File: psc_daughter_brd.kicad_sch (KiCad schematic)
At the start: 5 parts, among them J1 61082-061400LF

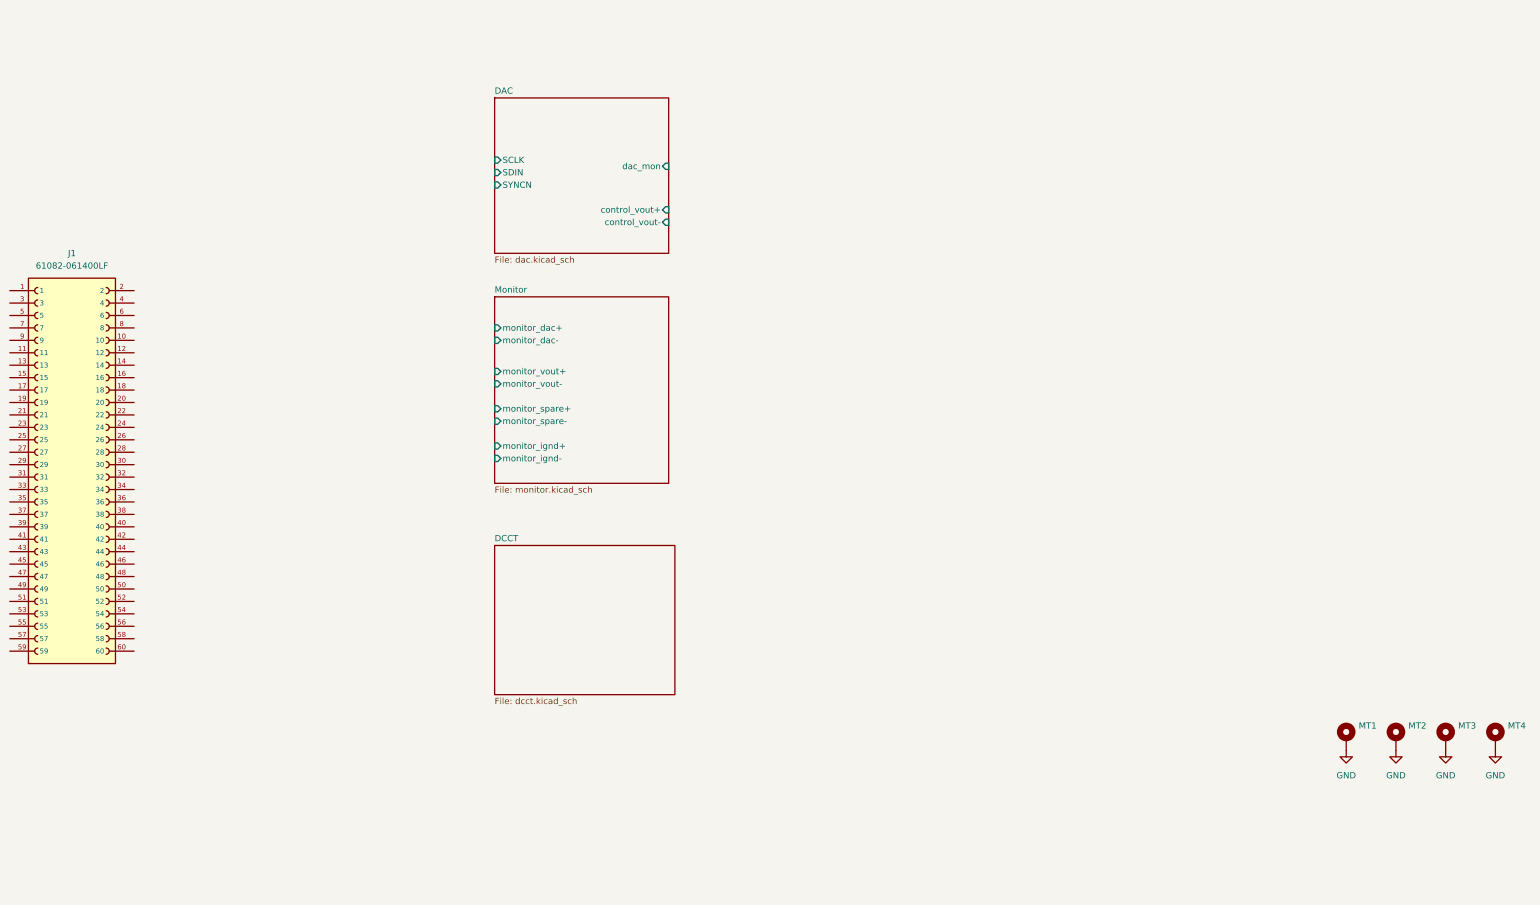
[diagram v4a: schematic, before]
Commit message: Add isolated digital I/O
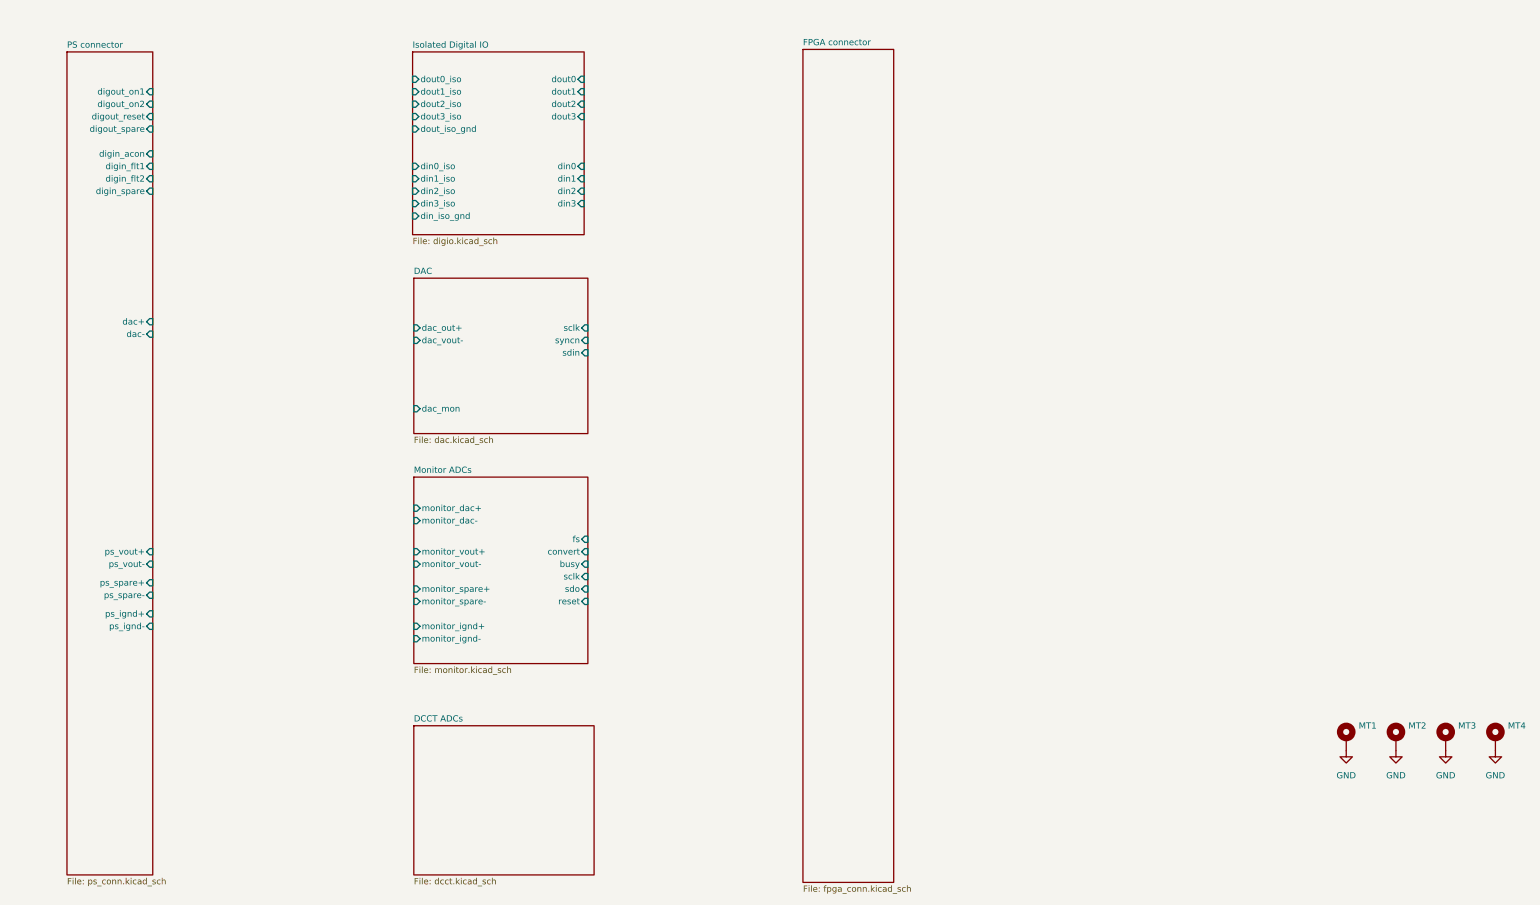
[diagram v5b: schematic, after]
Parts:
- removed J1: 61082-061400LF, myparts:AMPHENOL_61082-061400LF, symbol PSC:61082-061400LF
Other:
- sheet DCCT renamed DCCT ADCs
- sheet Monitor renamed Monitor ADCs
- added sheet FPGA connector (fpga_conn.kicad_sch)
- added sheet Isolated Digital IO (digio.kicad_sch)
- added sheet PS connector (ps_conn.kicad_sch)
- sheet DAC ports: added dac_out+, dac_vout-, sclk, sdin, syncn; removed SCLK, SDIN, SYNCN, control_vout+, control_vout-
- sheet Monitor ADCs ports: added busy, convert, fs, reset, sclk, sdo; removed none

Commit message: Add DCCT ADCs
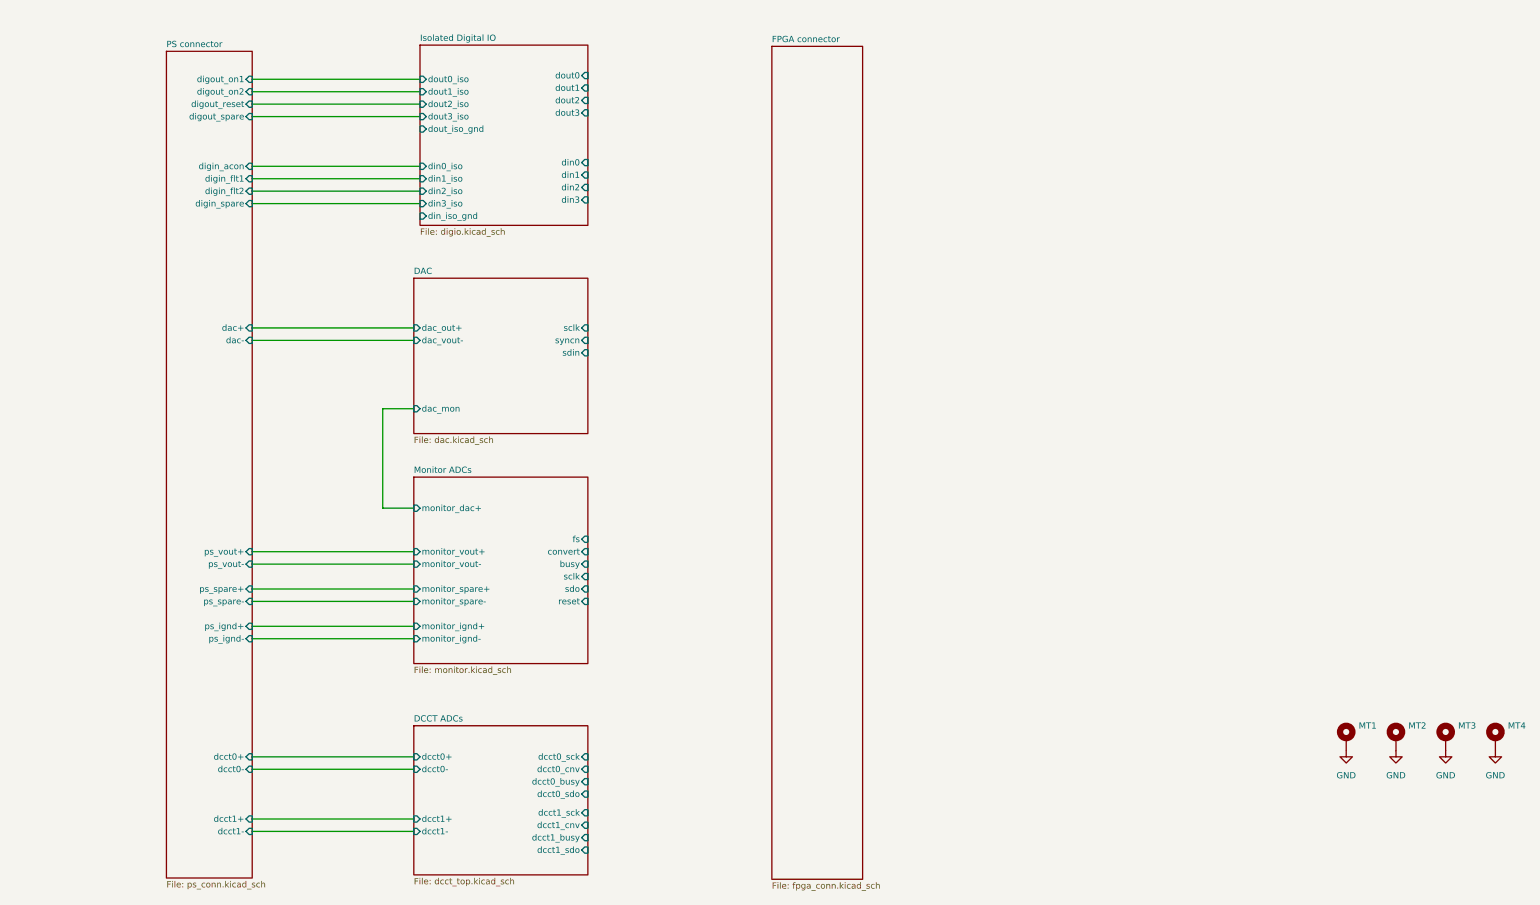
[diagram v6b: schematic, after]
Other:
- sheet DCCT ADCs: file dcct.kicad_sch -> dcct_top.kicad_sch
- sheet DCCT ADCs ports: added dcct0+, dcct0-, dcct0_busy, dcct0_cnv, dcct0_sck, dcct0_sdo, dcct1+, dcct1-, dcct1_busy, dcct1_cnv, dcct1_sck, dcct1_sdo; removed none
- sheet Monitor ADCs ports: added none; removed monitor_dac-
- sheet PS connector ports: added dcct0+, dcct0-, dcct1+, dcct1-; removed none

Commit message: DAC and DCCT placement
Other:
- sheet DCCT ADCs ports: added dcct_busy, dcct_cnv, dcct_sck; removed dcct0_busy, dcct0_cnv, dcct0_sck, dcct1_busy, dcct1_cnv, dcct1_sck
- sheet FPGA connector ports: added dac_sclk, dac_sdin, dac_syncn, dcct0_sdo, dcct1_sdo, dcct_busy, dcct_cnv, dcct_sck, din0, din1, din2, din3, dout0, dout1, dout2, dout3, mon_busy, mon_convert, mon_fs, mon_reset, mon_sclk, mon_sdo; removed none
- company: (none) -> BNL
- title: (none) -> Power Supply Controller

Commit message: finish rough placement
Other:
- sheet PS connector ports: added din_iso_gnd, dout_iso_gnd; removed none
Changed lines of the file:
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@@
 	(wire
 		(pts
-			(xy 128.27 74.93) (xy 162.56 74.93)
+			(xy 128.27 55.88) (xy 162.56 55.88)
 		)
 		(stroke
@@
 	(wire
 		(pts
-			(xy 128.27 62.23) (xy 162.56 62.23)
+			(xy 128.27 76.2) (xy 162.56 76.2)
 		)
 		(stroke
@@
 	(wire
 		(pts
+			(xy 128.27 81.28) (xy 162.56 81.28)
+		)
+		(stroke
+			(width 0)
+			(type default)
+		)
+	)
+	(wire
+		(pts
 			(xy 196.85 153.67) (xy 234.95 153.67)
 		)
@@
 	(wire
 		(pts
+			(xy 128.27 73.66) (xy 162.56 73.66)
+		)
+		(stroke
+			(width 0)
+			(type default)
+		)
+	)
+	(wire
+		(pts
 			(xy 196.85 105.41) (xy 234.95 105.41)
 		)
@@
 	(wire
 		(pts
-			(xy 128.27 57.15) (xy 162.56 57.15)
-		)
-		(stroke
-			(width 0)
-			(type default)
-		)
-	)
-	(wire
-		(pts
 			(xy 196.85 54.61) (xy 234.95 54.61)
 		)
@@
 	(wire
 		(pts
-			(xy 128.27 54.61) (xy 162.56 54.61)
+			(xy 128.27 60.96) (xy 162.56 60.96)
 		)
 		(stroke
@@
 	(wire
 		(pts
-			(xy 128.27 72.39) (xy 162.56 72.39)
-		)
-		(stroke
-			(width 0)
-			(type default)
-		)
-	)
-	(wire
-		(pts
 			(xy 196.85 74.93) (xy 234.95 74.93)
 		)
@@
 	(wire
 		(pts
-			(xy 128.27 59.69) (xy 162.56 59.69)
-		)
-		(stroke
-			(width 0)
-			(type default)
-		)
-	)
-	(wire
-		(pts
 			(xy 196.85 72.39) (xy 234.95 72.39)
 		)
@@
 	(wire
 		(pts
+			(xy 128.27 78.74) (xy 162.56 78.74)
+		)
+		(stroke
+			(width 0)
+			(type default)
+		)
+	)
+	(wire
+		(pts
 			(xy 128.27 105.41) (xy 161.29 105.41)
 		)
@@
 	(wire
 		(pts
-			(xy 128.27 80.01) (xy 162.56 80.01)
-		)
-		(stroke
-			(width 0)
-			(type default)
-		)
-	)
-	(wire
-		(pts
 			(xy 196.85 158.75) (xy 234.95 158.75)
 		)
@@
 	(wire
 		(pts
+			(xy 128.27 58.42) (xy 162.56 58.42)
+		)
+		(stroke
+			(width 0)
+			(type default)
+		)
+	)
+	(wire
+		(pts
 			(xy 128.27 205.74) (xy 161.29 205.74)
 		)
@@
 	(wire
 		(pts
-			(xy 128.27 77.47) (xy 162.56 77.47)
-		)
-		(stroke
-			(width 0)
-			(type default)
-		)
-	)
-	(wire
-		(pts
-			(xy 161.925 64.77) (xy 162.56 64.77)
+			(xy 128.27 63.5) (xy 162.56 63.5)
 		)
 		(stroke
@@
 		)
 		(pin "digin_flt1" input
-			(at 128.27 74.93 0)
+			(at 128.27 76.2 0)
 			(effects
 				(font
@@
 		)
 		(pin "digout_on2" input
-			(at 128.27 57.15 0)
+			(at 128.27 58.42 0)
 			(effects
 				(font
@@
 		)
 		(pin "digin_spare" input
-			(at 128.27 80.01 0)
+			(at 128.27 81.28 0)
 			(effects
 				(font
@@
 		)
 		(pin "digin_flt2" input
-			(at 128.27 77.47 0)
+			(at 128.27 78.74 0)
 			(effects
 				(font
@@
 		)
 		(pin "digout_spare" input
-			(at 128.27 62.23 0)
+			(at 128.27 63.5 0)
 			(effects
 				(font
@@
 		)
 		(pin "digin_acon" input
-			(at 128.27 72.39 0)
+			(at 128.27 73.66 0)
 			(effects
 				(font
@@
 		)
 		(pin "digout_reset" input
-			(at 128.27 59.69 0)
+			(at 128.27 60.96 0)
 			(effects
 				(font
@@
 		)
 		(pin "digout_on1" input
-			(at 128.27 54.61 0)
+			(at 128.27 55.88 0)
 			(effects
 				(font
@@
 			)
 		)
-		(pin "dcct0+" output
+		(pin "din_iso_gnd" input
+			(at 128.27 83.82 0)
+			(effects
+				(font
+					(size 1.27 1.27)
+				)
+				(justify right)
+			)
+		)
+		(pin "dcct1+" input
+			(at 128.27 205.74 0)
+			(effects
+				(font
+					(size 1.27 1.27)
+				)
+				(justify right)
+			)
+		)
+		(pin "dout_iso_gnd" input
+			(at 128.27 66.04 0)
+			(effects
+				(font
+					(size 1.27 1.27)
+				)
+				(justify right)
+			)
+		)
+		(pin "dcct1-" input
+			(at 128.27 208.28 0)
+			(effects
+				(font
+					(size 1.27 1.27)
+				)
+				(justify right)
+			)
+		)
+		(pin "dcct0+" input
 			(at 128.27 193.04 0)
 			(effects
@@
 			)
 		)
-		(pin "dcct0-" output
+		(pin "dcct0-" input
 			(at 128.27 195.58 0)
 			(effects
 				(font
-					(size 1.27 1.27)
-				)
-				(justify right)
-			)
-		)
-		(pin "dcct1+" output
-			(at 128.27 205.74 0)
-			(effects
-				(font
-					(size 1.27 1.27)
-				)
-				(justify right)
-			)
-		)
-		(pin "dcct1-" output
-			(at 128.27 208.28 0)
-			(effects
-				(font
